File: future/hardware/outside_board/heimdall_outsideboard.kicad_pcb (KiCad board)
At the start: 2 copper layers, 41.7 x 44.5 mm, 15 parts, among them J1 Conn_01x09, J2 Conn_01x06, J3 Conn_01x01_Male, J4 Conn_01x01_Male, J5 Conn_01x01_Male, J6 Conn_01x01_Male, Q1 2N3904, Q2 2N7000

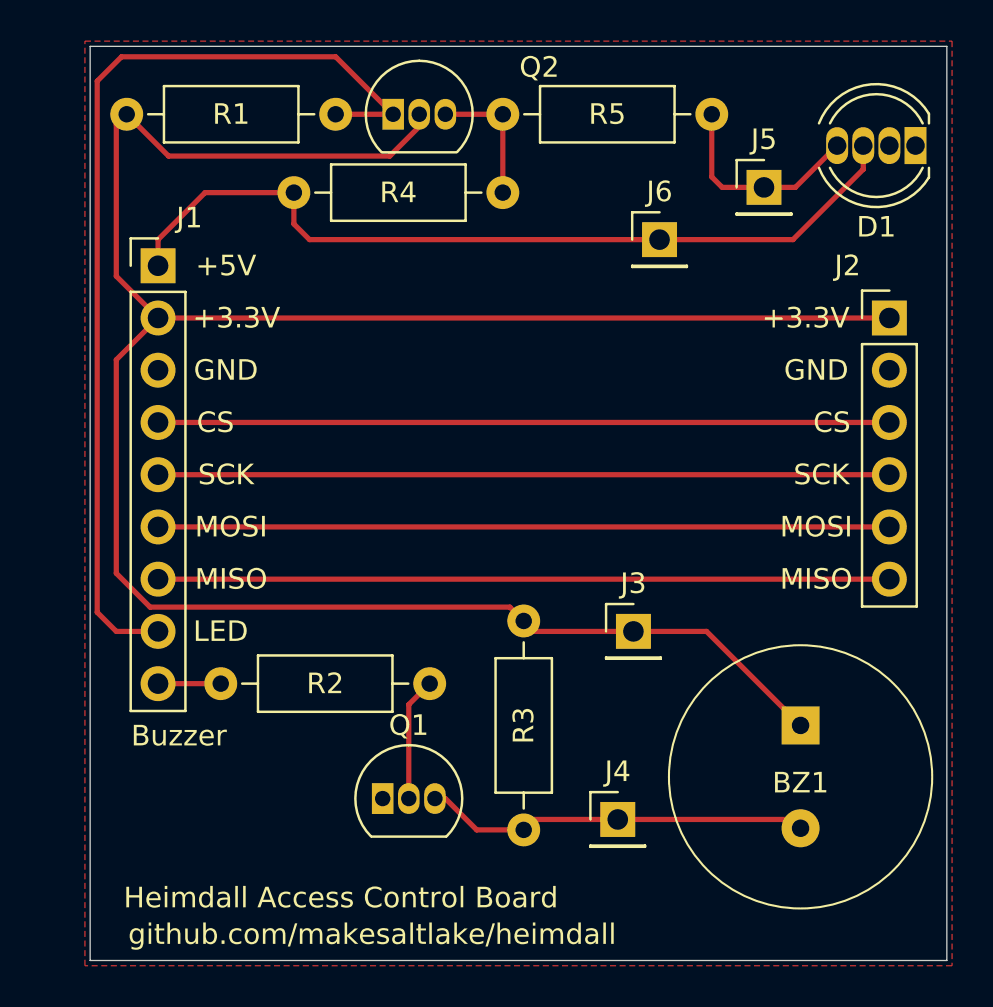
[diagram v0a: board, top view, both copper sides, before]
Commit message: Update future/hardware/outside_board for KiCad 6 and newest design
Update the files to KiCad 6 format.

Update schematic/pcb for the latest revision of the board that was sent
to Aisler for manufacturing and assembly.
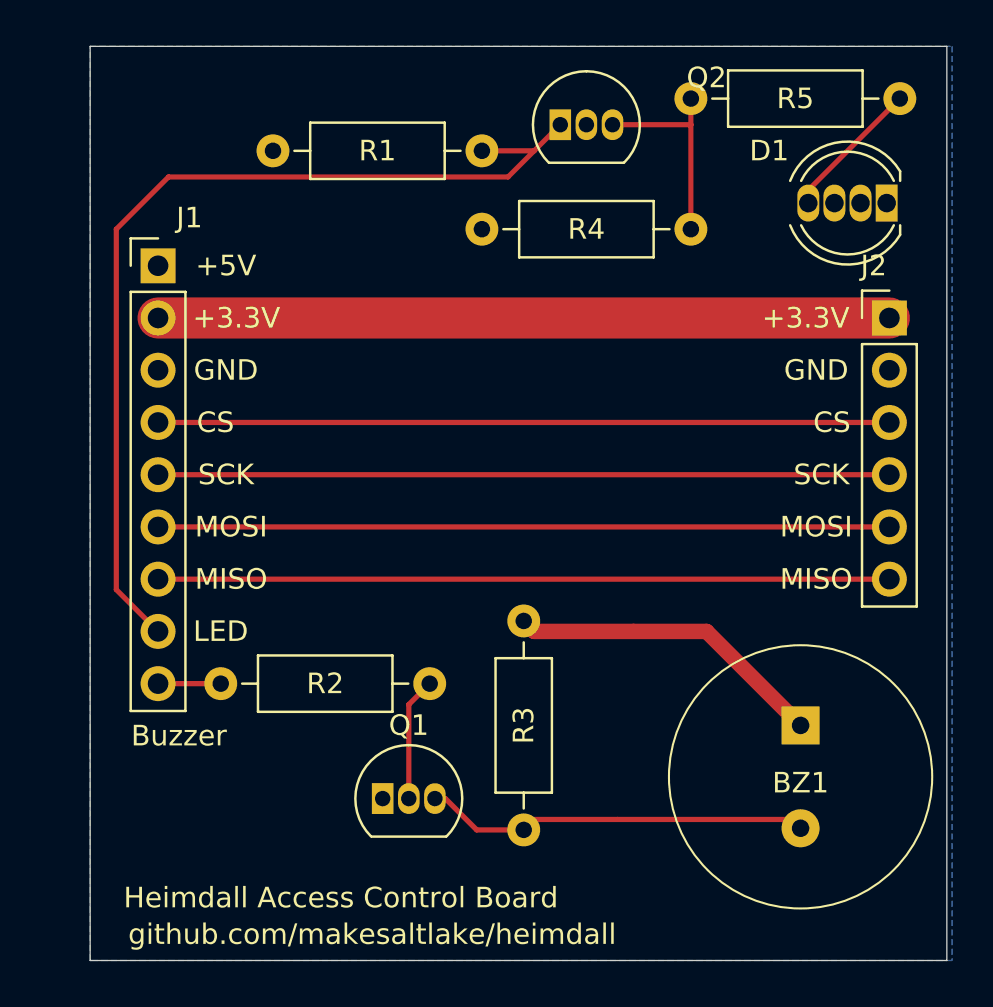
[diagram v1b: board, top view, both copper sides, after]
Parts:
- removed J3, J4, J5, J6: Conn_01x01_Male, Connector_PinHeader_2.54mm:PinHeader_1x01_P2.54mm_Vertical
- R5: value 470 -> 500
- moved R4 9.32 mm to (69.8, 85.1)
- moved R5 9.18 mm to (80.0, 78.7)
- moved Q2 8.14 mm to (73.7, 80.0)
- moved R1 7.33 mm to (69.8, 81.3)
- moved D1 3.13 mm to (89.5, 83.8)
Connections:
- D1 pad 1: Net-(D1-Pad1) -> unconnected-(D1-Pad1)
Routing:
- net +3V3: track 112.4 -> 51.1 mm
- net +5V: track 40.9 -> 0.00 mm
- net Net-(Q2-Pad3): track 6.60 -> 10.2 mm
- net Net-(R5-Pad2): track 10.2 -> 6.92 mm
- net /LED: track 48.0 -> 46.6 mm
- added copper zone on In1.Cu, net +3V3
- added copper zone on B.Cu, net +5V
- added copper zone on In2.Cu, net GND
- removed copper zone on F.Cu, net GND
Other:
- copper layers 2 -> 4
- net class Default removed
